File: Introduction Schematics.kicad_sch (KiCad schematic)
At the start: 1 part, among them U1 ESP32-S3-WROOM-1

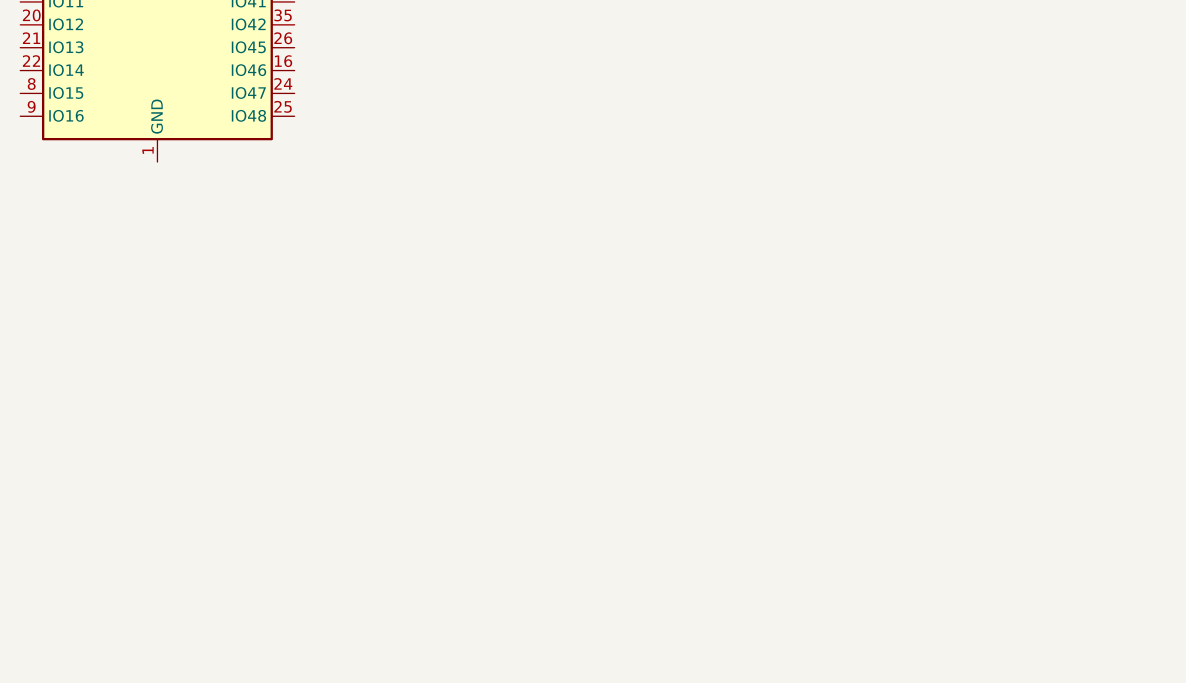
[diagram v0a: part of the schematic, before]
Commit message: SD added, Vss to Ground too
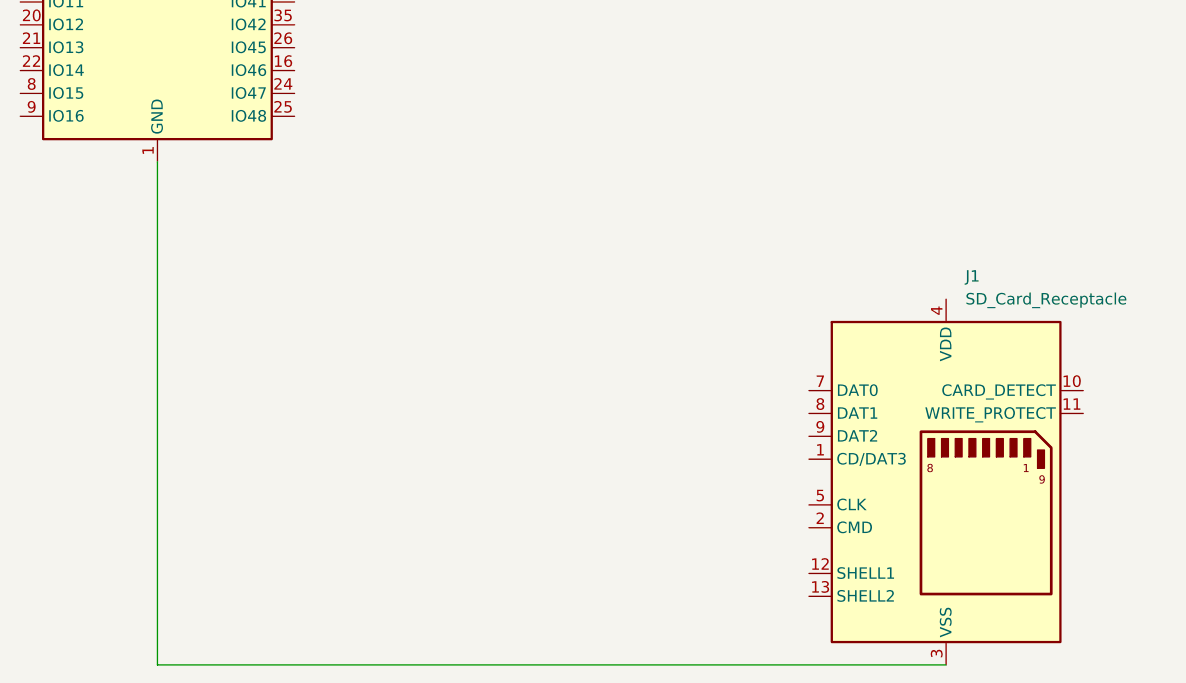
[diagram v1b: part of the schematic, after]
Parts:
- added J1: SD_Card_Receptacle, symbol Connector:SD_Card_Receptacle
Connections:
- net at U1.1 (GND), U1.40 (GND), U1.41 (GND): now also J1.3 (VSS), J1.6 (VSS)
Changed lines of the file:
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@@
 	(generator_version "9.0")
 	(paper "A4")
+	(wire
+		(pts
+			(xy 222.25 156.21) (xy 134.62 156.21)
+		)
+		(stroke
+			(width 0)
+			(type default)
+		)
+	)
+	(wire
+		(pts
+			(xy 134.62 156.21) (xy 134.62 100.33)
+		)
+		(stroke
+			(width 0)
+			(type default)
+		)
+	)
+	(symbol
+		(lib_id "Connector:SD_Card_Receptacle")
+		(at 222.25 135.89 0)
+		(unit 1)
+		(exclude_from_sim no)
+		(in_bom yes)
+		(on_board yes)
+		(dnp no)
+		(fields_autoplaced yes)
+		(property "Reference" "J1"
+			(at 224.3933 113.03 0)
+			(effects
+				(font
+					(size 1.27 1.27)
+				)
+				(justify left)
+			)
+		)
+		(property "Value" "SD_Card_Receptacle"
+			(at 224.3933 115.57 0)
+			(effects
+				(font
+					(size 1.27 1.27)
+				)
+				(justify left)
+			)
+		)
+		(property "Footprint" ""
+			(at 231.14 139.192 0)
+			(effects
+				(font
+					(size 1.27 1.27)
+				)
+				(hide yes)
+			)
+		)
+		(property "Datasheet" "http://portal.fciconnect.com/Comergent//fci/drawing/10067847.pdf"
+			(at 222.25 135.89 0)
+			(effects
+				(font
+					(size 1.27 1.27)
+				)
+				(hide yes)
+			)
+		)
+		(property "Description" "SD card receptacle"
+			(at 222.25 135.89 0)
+			(effects
+				(font
+					(size 1.27 1.27)
+				)
+				(hide yes)
+			)
+		)
+		(pin "4"
+		)
+		(pin "13"
+		)
+		(pin "10"
+		)
+		(pin "9"
+		)
+		(pin "8"
+		)
+		(pin "1"
+		)
+		(pin "6"
+		)
+		(pin "7"
+		)
+		(pin "11"
+		)
+		(pin "2"
+		)
+		(pin "5"
+		)
+		(pin "3"
+		)
+		(pin "12"
+		)
+		(instances
+			(project ""
+				(path "/f2ac59a6-0e60-42dc-a6ba-aac143aff5be"
+					(reference "J1")
+					(unit 1)
+				)
+			)
+		)
+	)
 	(symbol
 		(lib_id "RF_Module:ESP32-S3-WROOM-1")

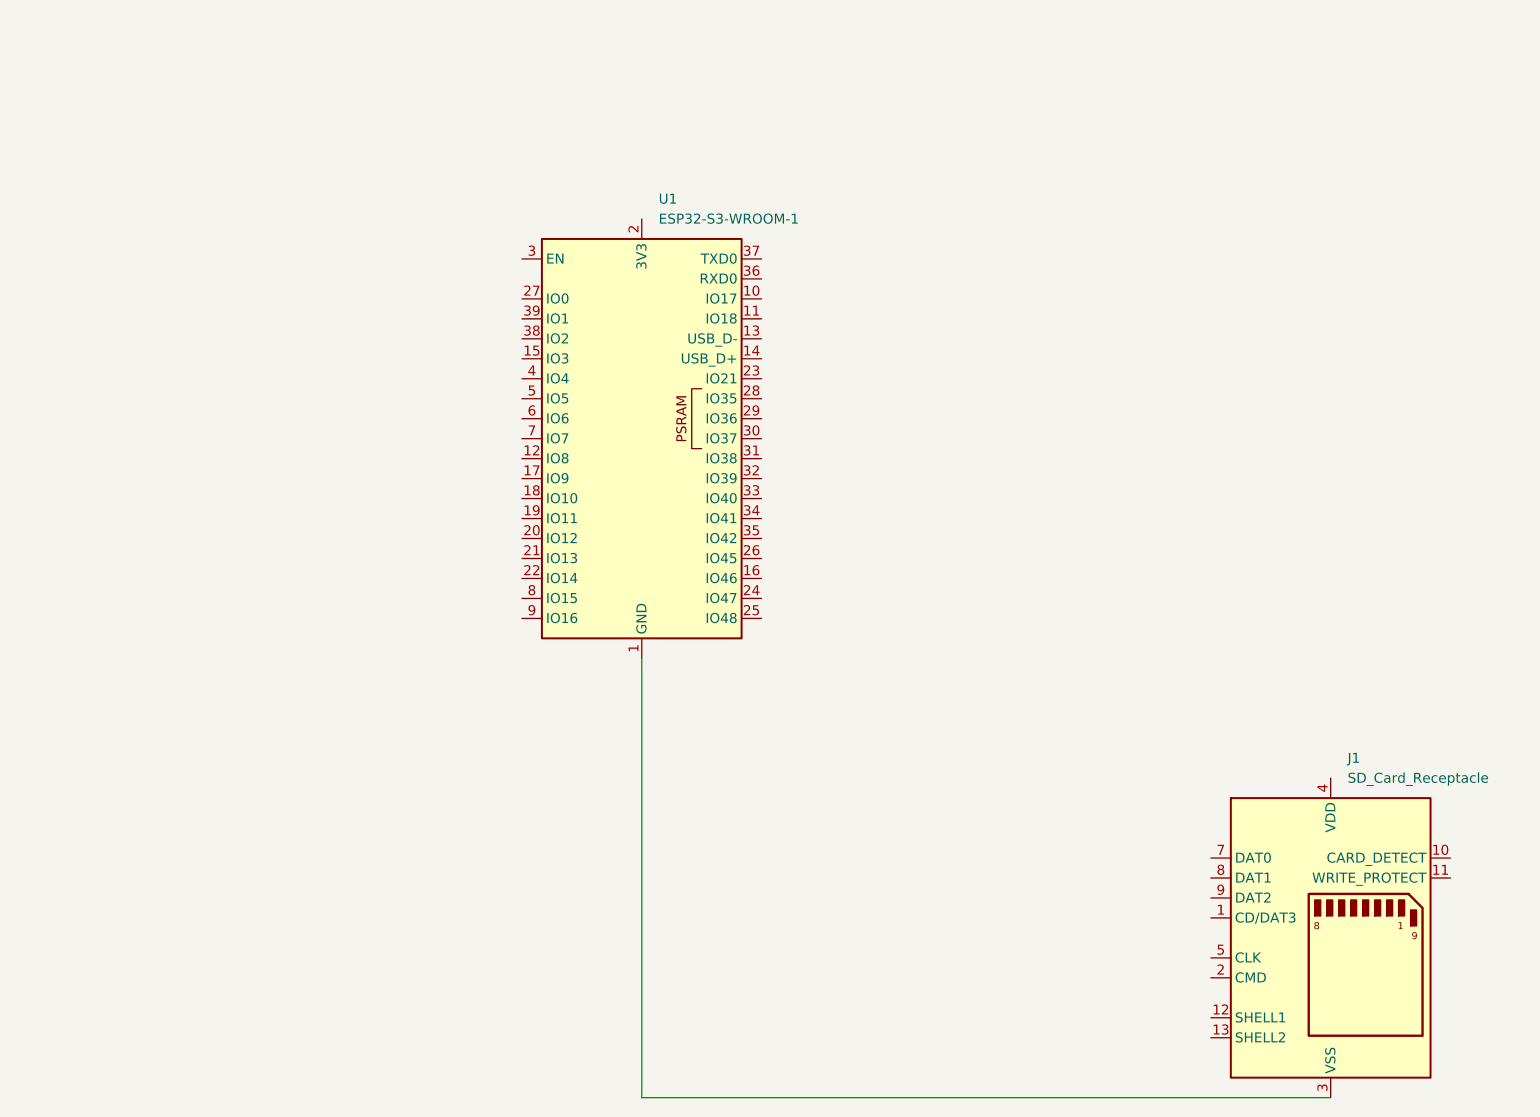
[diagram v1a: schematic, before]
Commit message: SD connections to ESP32 added
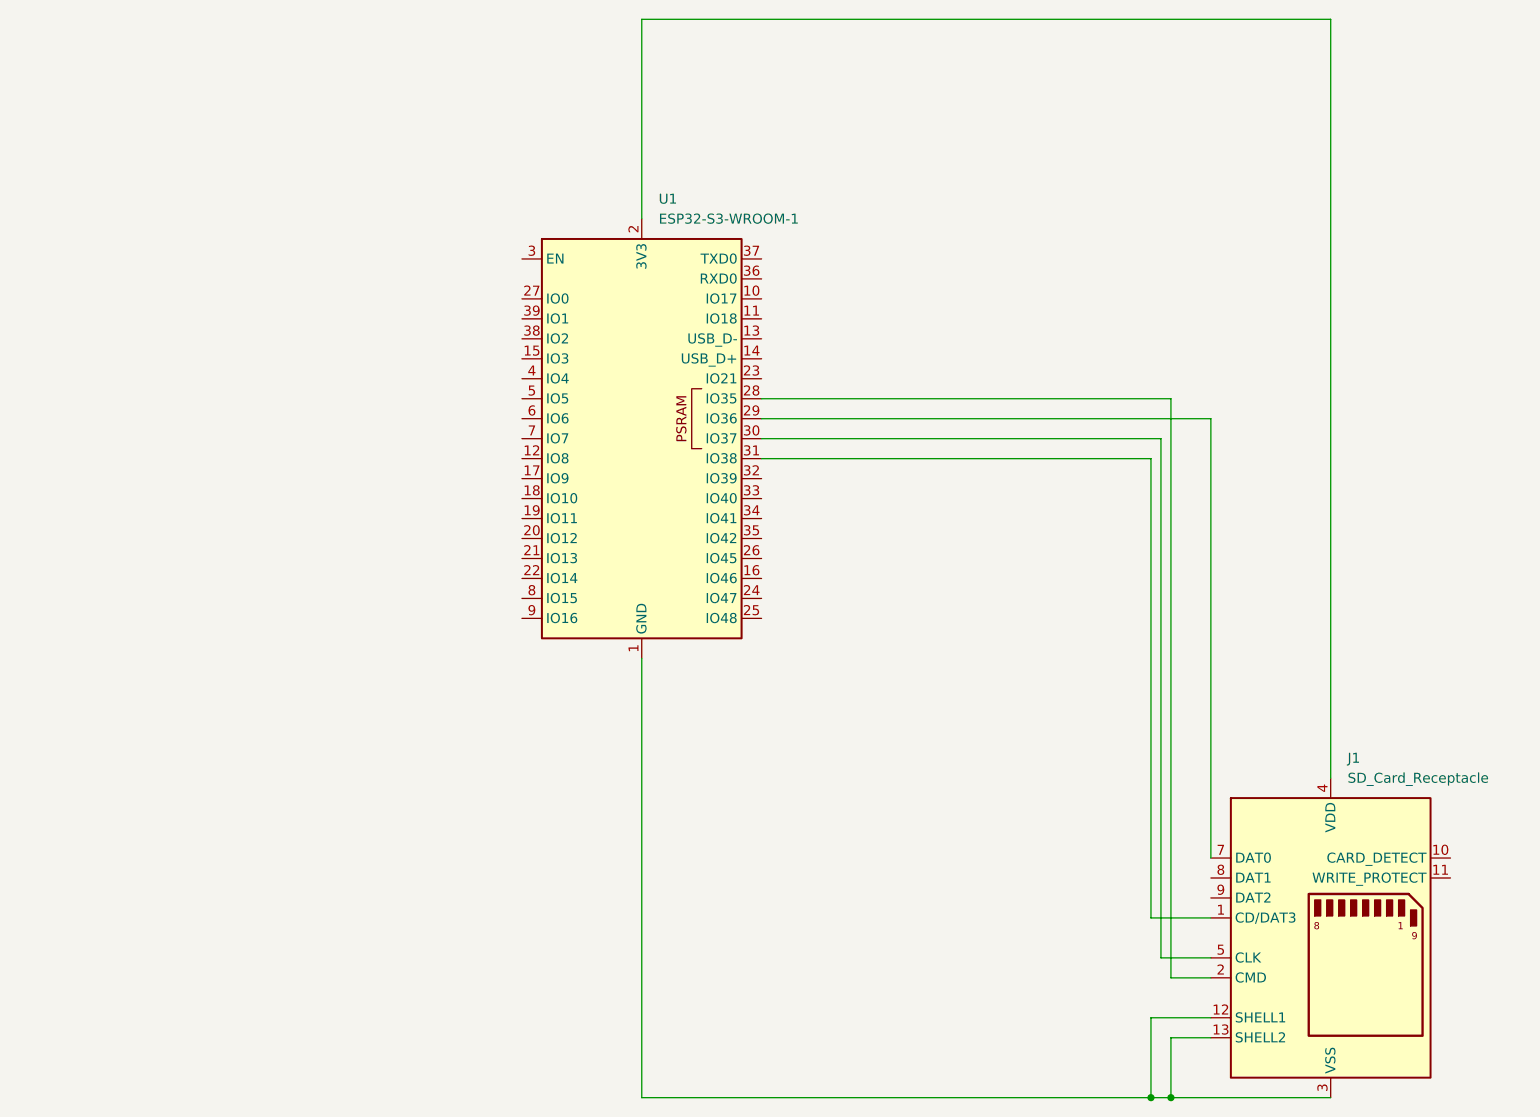
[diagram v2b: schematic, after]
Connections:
- net at J1.1 (CD/DAT3): now also U1.31 (IO38)
- net at J1.12 (SHELL1): now also J1.13 (SHELL2), J1.3 (VSS), J1.6 (VSS), U1.1 (GND), U1.40 (GND), U1.41 (GND)
- net at J1.2 (CMD): now also U1.28 (IO35)
- net at J1.4 (VDD): now also U1.2 (3V3)
- net at J1.5 (CLK): now also U1.30 (IO37)
- net at J1.7 (DAT0): now also U1.29 (IO36)
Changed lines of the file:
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@@
 	(generator_version "9.0")
 	(paper "A4")
-	(wire
-		(pts
-			(xy 222.25 156.21) (xy 134.62 156.21)
+	(junction
+		(at 199.39 156.21)
+		(diameter 0)
+		(color 0 0 0 0)
+	)
+	(junction
+		(at 201.93 156.21)
+		(diameter 0)
+		(color 0 0 0 0)
+	)
+	(wire
+		(pts
+			(xy 201.93 156.21) (xy 199.39 156.21)
+		)
+		(stroke
+			(width 0)
+			(type default)
+		)
+	)
+	(wire
+		(pts
+			(xy 199.39 133.35) (xy 199.39 74.93)
+		)
+		(stroke
+			(width 0)
+			(type default)
+		)
+	)
+	(wire
+		(pts
+			(xy 200.66 72.39) (xy 200.66 138.43)
+		)
+		(stroke
+			(width 0)
+			(type default)
+		)
+	)
+	(wire
+		(pts
+			(xy 222.25 19.05) (xy 134.62 19.05)
+		)
+		(stroke
+			(width 0)
+			(type default)
+		)
+	)
+	(wire
+		(pts
+			(xy 199.39 74.93) (xy 149.86 74.93)
+		)
+		(stroke
+			(width 0)
+			(type default)
+		)
+	)
+	(wire
+		(pts
+			(xy 199.39 146.05) (xy 199.39 156.21)
+		)
+		(stroke
+			(width 0)
+			(type default)
+		)
+	)
+	(wire
+		(pts
+			(xy 207.01 125.73) (xy 207.01 69.85)
+		)
+		(stroke
+			(width 0)
+			(type default)
+		)
+	)
+	(wire
+		(pts
+			(xy 207.01 140.97) (xy 201.93 140.97)
+		)
+		(stroke
+			(width 0)
+			(type default)
+		)
+	)
+	(wire
+		(pts
+			(xy 134.62 19.05) (xy 134.62 44.45)
+		)
+		(stroke
+			(width 0)
+			(type default)
+		)
+	)
+	(wire
+		(pts
+			(xy 222.25 156.21) (xy 201.93 156.21)
+		)
+		(stroke
+			(width 0)
+			(type default)
+		)
+	)
+	(wire
+		(pts
+			(xy 199.39 156.21) (xy 134.62 156.21)
+		)
+		(stroke
+			(width 0)
+			(type default)
+		)
+	)
+	(wire
+		(pts
+			(xy 201.93 140.97) (xy 201.93 67.31)
+		)
+		(stroke
+			(width 0)
+			(type default)
+		)
+	)
+	(wire
+		(pts
+			(xy 201.93 148.59) (xy 201.93 156.21)
+		)
+		(stroke
+			(width 0)
+			(type default)
+		)
+	)
+	(wire
+		(pts
+			(xy 207.01 146.05) (xy 199.39 146.05)
+		)
+		(stroke
+			(width 0)
+			(type default)
+		)
+	)
+	(wire
+		(pts
+			(xy 200.66 138.43) (xy 207.01 138.43)
+		)
+		(stroke
+			(width 0)
+			(type default)
+		)
+	)
+	(wire
+		(pts
+			(xy 207.01 69.85) (xy 149.86 69.85)
+		)
+		(stroke
+			(width 0)
+			(type default)
+		)
+	)
+	(wire
+		(pts
+			(xy 207.01 133.35) (xy 199.39 133.35)
+		)
+		(stroke
+			(width 0)
+			(type default)
+		)
+	)
+	(wire
+		(pts
+			(xy 201.93 67.31) (xy 149.86 67.31)
+		)
+		(stroke
+			(width 0)
+			(type default)
+		)
+	)
+	(wire
+		(pts
+			(xy 222.25 115.57) (xy 222.25 19.05)
 		)
 		(stroke
@@
 		)
 		(stroke
+			(width 0)
+			(type default)
+		)
+	)
+	(wire
+		(pts
+			(xy 149.86 72.39) (xy 200.66 72.39)
+		)
+		(stroke
+			(width 0)
+			(type default)
+		)
+	)
+	(wire
+		(pts
+			(xy 207.01 148.59) (xy 201.93 148.59)
+		)
+		(stroke

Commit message: UART 1 & 2 , I2C 1 & 2 added
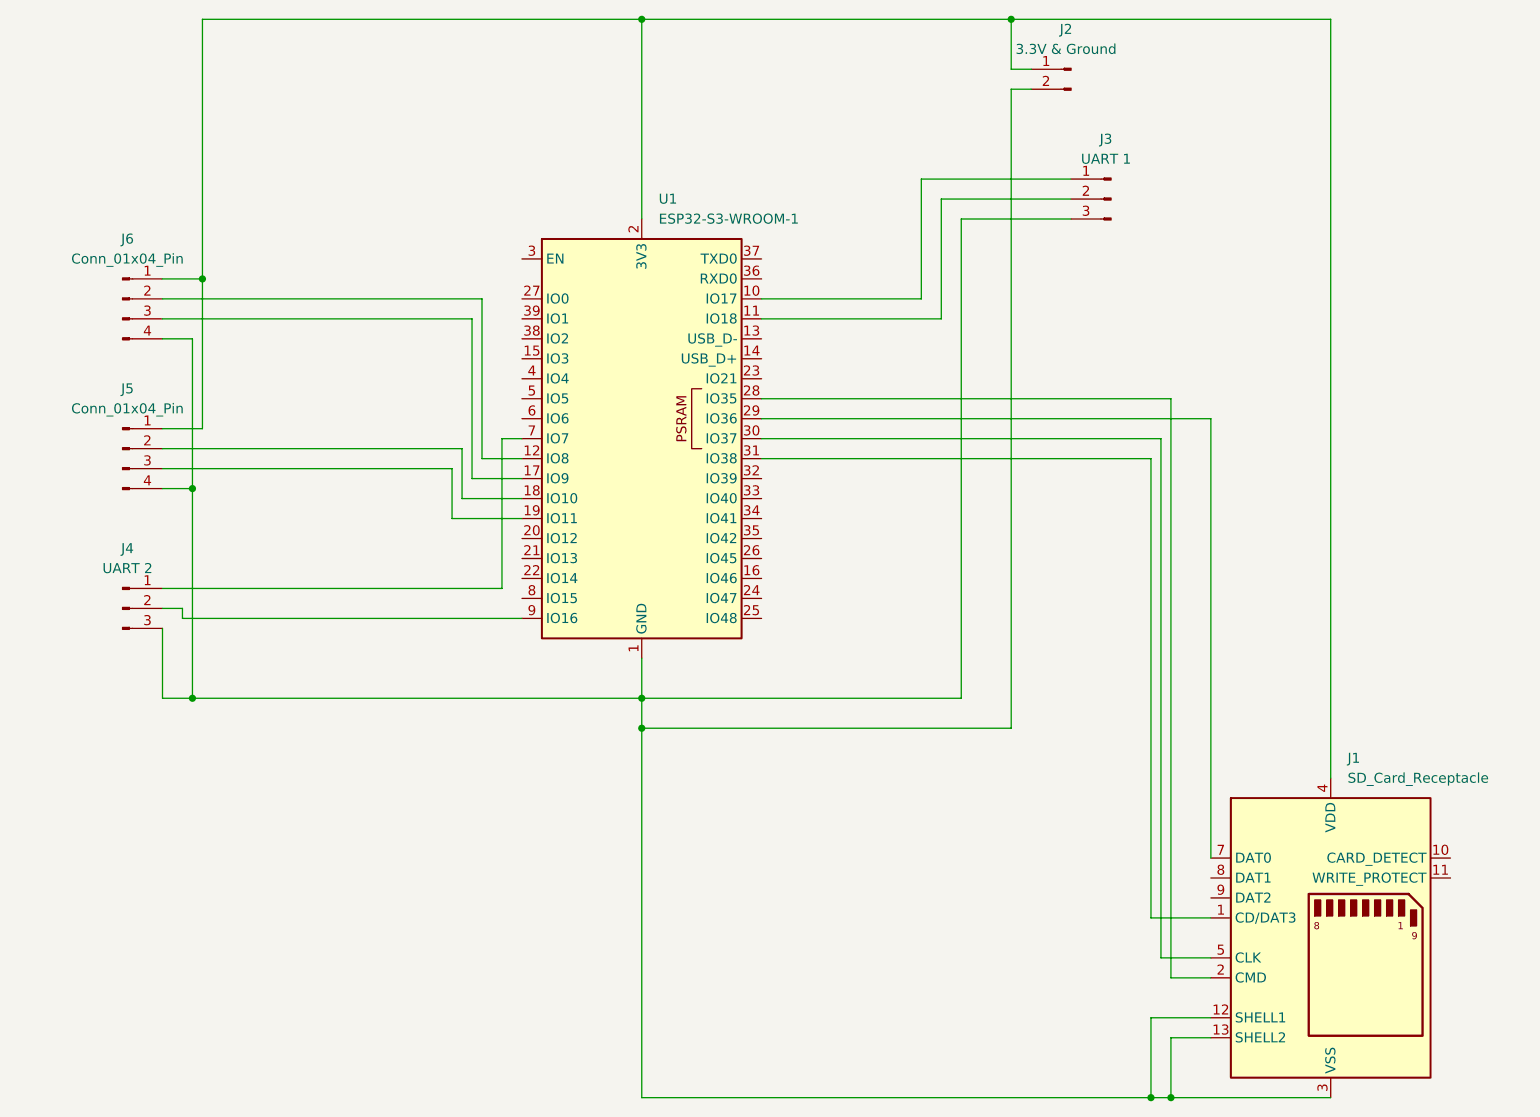
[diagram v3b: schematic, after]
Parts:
- added J2: 3.3V & Ground, symbol Connector:Conn_01x02_Pin
- added J3: UART 1, symbol Connector:Conn_01x03_Pin
- added J4: UART 2, symbol Connector:Conn_01x03_Pin
- added J5, J6: Conn_01x04_Pin, symbol Connector:Conn_01x04_Pin
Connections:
- net at J1.12 (SHELL1), J1.13 (SHELL2), J1.3 (VSS)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: now also J2.2 (Pin_2), J3.3 (Pin_3), J4.3 (Pin_3), J5.4 (Pin_4), J6.4 (Pin_4)
- net at J1.4 (VDD), U1.2 (3V3): now also J2.1 (Pin_1), J5.1 (Pin_1), J6.1 (Pin_1)
- net at U1.10 (IO17): now also J3.1 (Pin_1)
- net at U1.11 (IO18): now also J3.2 (Pin_2)
- net at U1.12 (IO8): now also J6.2 (Pin_2)
- net at U1.17 (IO9): now also J6.3 (Pin_3)
- net at U1.18 (IO10): now also J5.2 (Pin_2)
- net at U1.19 (IO11): now also J5.3 (Pin_3)
- net at U1.7 (IO7): now also J4.1 (Pin_1)
- net at U1.9 (IO16): now also J4.2 (Pin_2)

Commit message: SPI Added
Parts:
- added J7: SPI, symbol Connector:Conn_01x06_Pin
- J5: value Conn_01x04_Pin -> I2C 2
- J6: value Conn_01x04_Pin -> I2C 1
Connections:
- net at J1.12 (SHELL1), J1.13 (SHELL2), J1.3 (VSS)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: now also J7.6 (Pin_6)
- net at J1.4 (VDD), J2.1 (Pin_1), J5.1 (Pin_1)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: now also J7.1 (Pin_1)
- net at U1.20 (IO12): now also J7.2 (Pin_2)
- net at U1.21 (IO13): now also J7.3 (Pin_3)
- net at U1.22 (IO14): now also J7.4 (Pin_4)
- net at U1.8 (IO15): now also J7.5 (Pin_5)

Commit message: Thrusters Added
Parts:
- added J8: Thrusters, symbol Connector:Conn_01x08_Pin
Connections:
- net at J1.5 (CLK), U1.30 (IO37): now also U1.32 (IO39), J8.1 (Pin_1)
- net at U1.16 (IO46): now also J8.6 (Pin_6)
- net at U1.24 (IO47): now also J8.7 (Pin_7)
- net at U1.25 (IO48): now also J8.8 (Pin_8)
- net at U1.26 (IO45): now also J8.5 (Pin_5)
- net at U1.33 (IO40): now also J8.2 (Pin_2)
- net at U1.34 (IO41): now also J8.3 (Pin_3)
- net at U1.35 (IO42): now also J8.4 (Pin_4)
